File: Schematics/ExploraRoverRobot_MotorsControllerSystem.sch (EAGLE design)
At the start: 15 parts, among them X1 Power supply (7.4V)

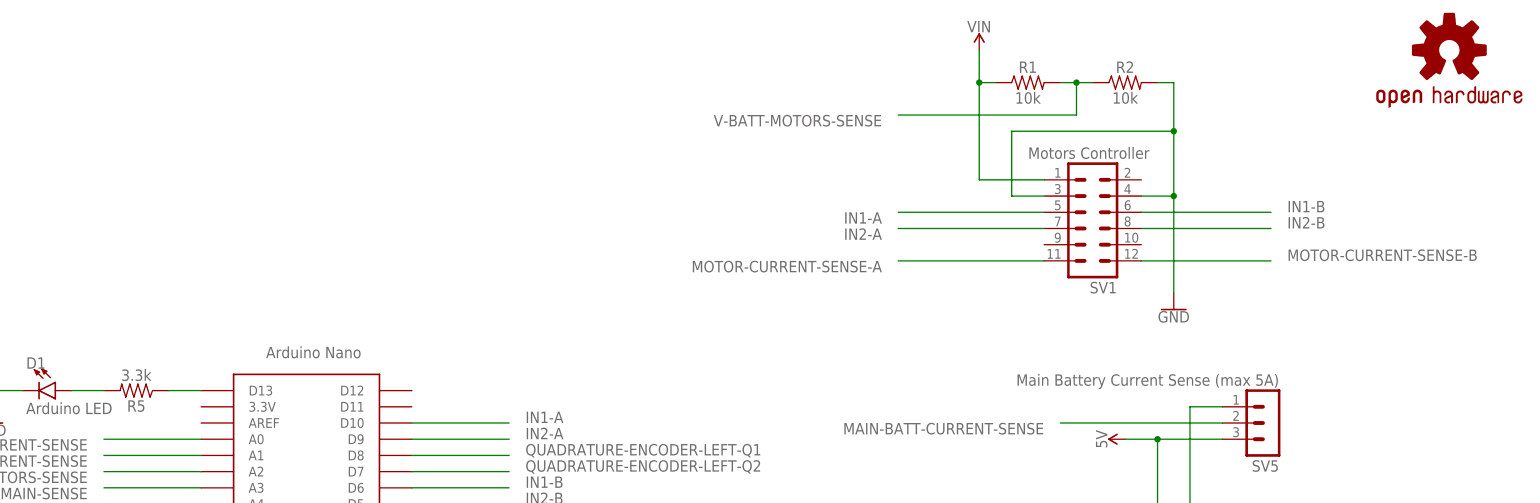
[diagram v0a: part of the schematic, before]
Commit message: Add motors controller system block diagram
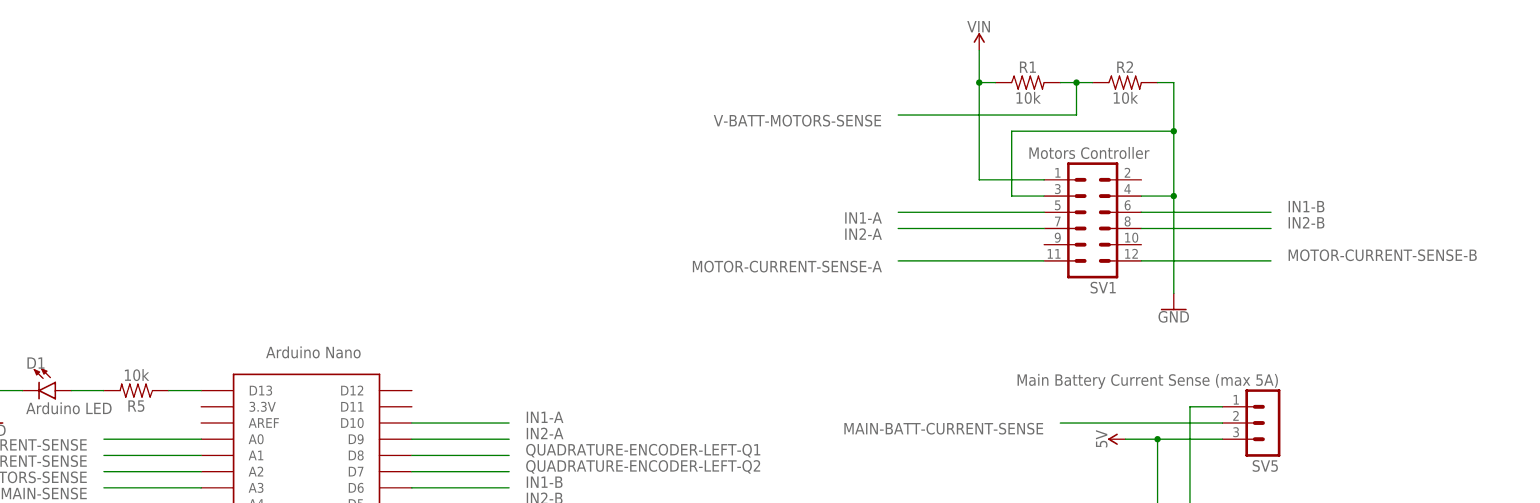
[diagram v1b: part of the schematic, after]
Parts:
- removed LOGO1: OSHW-LOGOL, SparkFun-Aesthetics:OSHW-LOGOL
- R1, R2, R3, R4: device SparkFun-Resistors:10KOHM-0603-1/10W-1% -> SparkFun-Resistors:10KOHM-HORIZ-1/6W-5%
- R5: value 3.3k -> 10k; device SparkFun-Resistors:10KOHM-0603-1/10W-1% -> SparkFun-Resistors:10KOHM-HORIZ-1/4W-1%
